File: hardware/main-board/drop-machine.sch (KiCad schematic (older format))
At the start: 29 parts, among them J1 Power in, J2 User interface, J3 Isp_conn, J4 CONN_01X06, J5 Conn_01x03, Q1 2N7000, Q2 2N7000, Q3 2N7000, Q4 2N7000, Q5 2N7000, Q6 2N7000, Q7 2N7000, SW1 On_off, U1 ATTINY2313-20PU, U2 7805

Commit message: Start with drop machine revision 2: Update to use Atmega162 that has enough pins for 19 valves. Add user interface connection with external indicator and button for flushing.
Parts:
- removed C1: 1 uF, symbol CP
- removed C2: 100 nF, symbol C
- removed J2: User interface, symbol Conn_01x03
- removed J3: Isp_conn, symbol CONN_02X03
- removed J4: CONN_01X06, symbol CONN_01X06
- removed J5: Conn_01x03, symbol Conn_01x03
- removed U1: ATTINY2313-20PU, Housings_DIP:DIP-20_W7.62mm, symbol ATTINY2313-20PU
- removed U2: 7805, symbol 7805_oturpe
- added C?: 100 nF, symbol drop-machine-rescue:C
- added C?: 330 nF, symbol drop-machine-rescue:C
- added C?: C, symbol drop-machine-rescue:C
- added C? (x2): 12 pF, symbol drop-machine-rescue:C
- added J?: Valves, symbol drop-machine-rescue:Conn_02x13_Counter_Clockwise
- added J?: CAN bus, symbol drop-machine-rescue:Screw_Terminal_1x02
- added J?: User interface, symbol Connector:Conn_01x06_Male
- added P?: isp_interface, symbol oturpe-kicad-lib:isp_interface
- added Q? (x12): 2N7000, symbol drop-machine-rescue:Q_NMOS_SGD
- added R?: R, symbol drop-machine-rescue:R
- added R? (x12): 100, symbol drop-machine-rescue:R
- added R?: 10k, symbol Device:R
- added U?: ATMEGA162-16PU, DIL40, symbol drop-machine-rescue:ATMEGA162-16PU
- added U?: MCP2515-I/ST, Housings_SSOP:TSSOP-20_4.4x6.5mm_Pitch0.65mm, symbol drop-machine-rescue:MCP2515-I_ST
- added U?: MCP2551-I/P, Housings_DIP:DIP-8_W7.62mm, symbol drop-machine-rescue:MCP2551-I_P
- added U?: 7805_oturpe, symbol oturpe-kicad-lib:7805_oturpe
- added Y?: 6 Mhz, symbol drop-machine-rescue:Crystal
- C3: symbol C -> drop-machine-rescue:C
- D1: symbol D -> drop-machine-rescue:D
- D2: symbol LED -> drop-machine-rescue:LED
- J1: symbol Screw_Terminal_1x02 -> drop-machine-rescue:Screw_Terminal_1x02
- Q1, Q2, Q3, Q4, Q5, Q6, Q7: symbol Q_NMOS_SGD -> drop-machine-rescue:Q_NMOS_SGD
- R1, R2, R3, R4, R5, R6, R7, R8, R9: symbol R -> drop-machine-rescue:R
- SW1: symbol SW_SPST-RESCUE-drop-machine -> drop-machine-rescue:SW_SPST-RESCUE-drop-machine
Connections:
- net +12V: now also C?.1, U?.1 (VI)
- net +5V: now also C?.1, P?.2 (Vcc), R?.1, R?.2, U?.20 (VDD), U?.3 (VDD), U?.3 (VO), U?.40 (VCC)
- net GND: now also C?.2, C?.2, C?.2, C?.2, C?.2, J?.1 (Pin_1), J?.14 (Pin_14), J?.15 (Pin_15), J?.17 (Pin_17), J?.19 (Pin_19), J?.21 (Pin_21), J?.23 (Pin_23), J?.25 (Pin_25), P?.6 (GND), Q?.1 (S), Q?.1 (S), Q?.1 (S), Q?.1 (S), Q?.1 (S), Q?.1 (S), Q?.1 (S), Q?.1 (S), Q?.1 (S), Q?.1 (S), Q?.1 (S), Q?.1 (S), U?.10 (VSS), U?.2 (GND), U?.2 (VSS), U?.20 (GND), U?.8 (Rs)
- net at R1.2, R2.2: now also U?.30 (PE1(ALE))
- net U1.0: now reaches Q1.3 (D)
- net U1.0: now also J?.2 (Pin_2)
- net U1.1: now reaches Q2.3 (D)
- net U1.1: now also J?.3 (Pin_3)
- net U1.2: now reaches Q3.3 (D)
- net U1.2: now also J?.4 (Pin_4)
- net U1.3: now reaches Q4.3 (D)
- net U1.3: now also J?.5 (Pin_5)
- net U1.4: now reaches Q5.3 (D)
- net U1.4: now also J?.6 (Pin_6)
- net at R1.1: now also J?.2 (Pin_2)
- net U1.5: now reaches Q6.3 (D)
- net U1.5: now also J?.7 (Pin_7)
- net U0.0: now reaches Q7.3 (D)
- net U0.0: now also J?.1 (Pin_1)
- net V0 renamed V1.0
- net V1.0: now also U?.3 ((RXD1/AIN0)PB2)
- net V1 renamed V1.1
- net V1.1: now also U?.4 ((TXD1/AIN1)PB3)
- net V2 renamed V1.2
- net V1.2: now also U?.21 ((PCINT8/A8)PC0)
- net V3 renamed V1.3
- net V1.3: now also U?.22 ((PCINT9/A9)PC1)
- net V4 renamed V1.4
- net V1.4: now also U?.23 ((PCINT10/A10)PC2)
- net V5 renamed V1.5
- net V1.5: now also U?.24 ((PCINT11/A11)PC3)
- net V6 renamed V0.0
- net V0.0: now also U?.2 ((OC2/T1)PB1)
- new net: U?.1 ((OC0/T0)PB0), U?.9 (OSC1)
- new net: C?.1, U?.18 (XTAL2), Y?.1
- new net: C?.1, U?.19 (XTAL1), Y?.2
- new net: J?.3 (Pin_3), U?.29 (PE2(OC1B))
- new net: P?.5 (Reset), U?.9 (~RESET)
- new net: U?.1 (TXCAN), U?.1 (TXD)
- new net: C?.1, R?.2, U?.19 (~RESET)
- new net: U?.2 (RXCAN), U?.4 (RXD)
- new net: Q?.2 (G), R?.2 (x12)
- new net: J?.2, U?.6 (CANL)
- new net: J?.1, U?.7 (CANH)
- new net MISO: P?.1 (MISO), U?.17 (SO), U?.7 ((MISO)PB6)
- new net MOSI: P?.4 (MOSI), U?.16 (SI), U?.6 ((MOSI)PB5)
- new net SCK: P?.3 (SCK), U?.14 (SCK), U?.8 ((SCK)PB7)
- new net U2.0: J?.8 (Pin_8), Q?.3 (D)
- new net U2.1: J?.9 (Pin_9), Q?.3 (D)
- new net U2.10: J?.18 (Pin_18), Q?.3 (D)
- new net U2.11: J?.16 (Pin_16), Q?.3 (D)
- new net U2.2: J?.10 (Pin_10), Q?.3 (D)
- new net U2.3: J?.11 (Pin_11), Q?.3 (D)
- new net U2.4: J?.12 (Pin_12), Q?.3 (D)
- new net U2.5: J?.13 (Pin_13), Q?.3 (D)
- new net U2.6: J?.26 (Pin_26), Q?.3 (D)
- new net U2.7: J?.24 (Pin_24), Q?.3 (D)
- new net U2.8: J?.22 (Pin_22), Q?.3 (D)
- new net U2.9: J?.20 (Pin_20), Q?.3 (D)
- new net V2.0: R?.1, U?.25 ((PCINT12/TCK/A12)PC4)
- new net V2.1: R?.1, U?.26 ((PCINT13/TMS/A13)PC5)
- new net V2.10: R?.1, U?.16 ((~WR~)PD6)
- new net V2.11: R?.1, U?.17 ((~RD~)PD7)
- new net V2.2: R?.1, U?.27 ((PCINT14/TDO/A14)PC6)
- new net V2.3: R?.1, U?.28 ((PCINT15/TDI/A15)PC7)
- new net V2.4: R?.1, U?.10 ((RXD0)PD0)
- new net V2.5: R?.1, U?.11 ((TXD0)PD1)
- new net V2.6: R?.1, U?.12 ((XCK1/INT0)PD2)
- new net V2.7: R?.1, U?.13 ((ICP3/INT1)PD3)
- new net V2.8: R?.1, U?.14 ((XCK0/OC3A/TOSC1)PD4)
- new net V2.9: R?.1, U?.15 ((OC1A/TOSC2)PD5)
- new net ~SS: R?.1, U?.18 (~CS), U?.5 ((OC3B/~SS~)PB4)
- no-connect marks 5 -> 4
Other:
- moved on the sheet: C3, D1, D2, J1, Q1, Q2, Q3, Q4, Q5, Q6, Q7, R1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

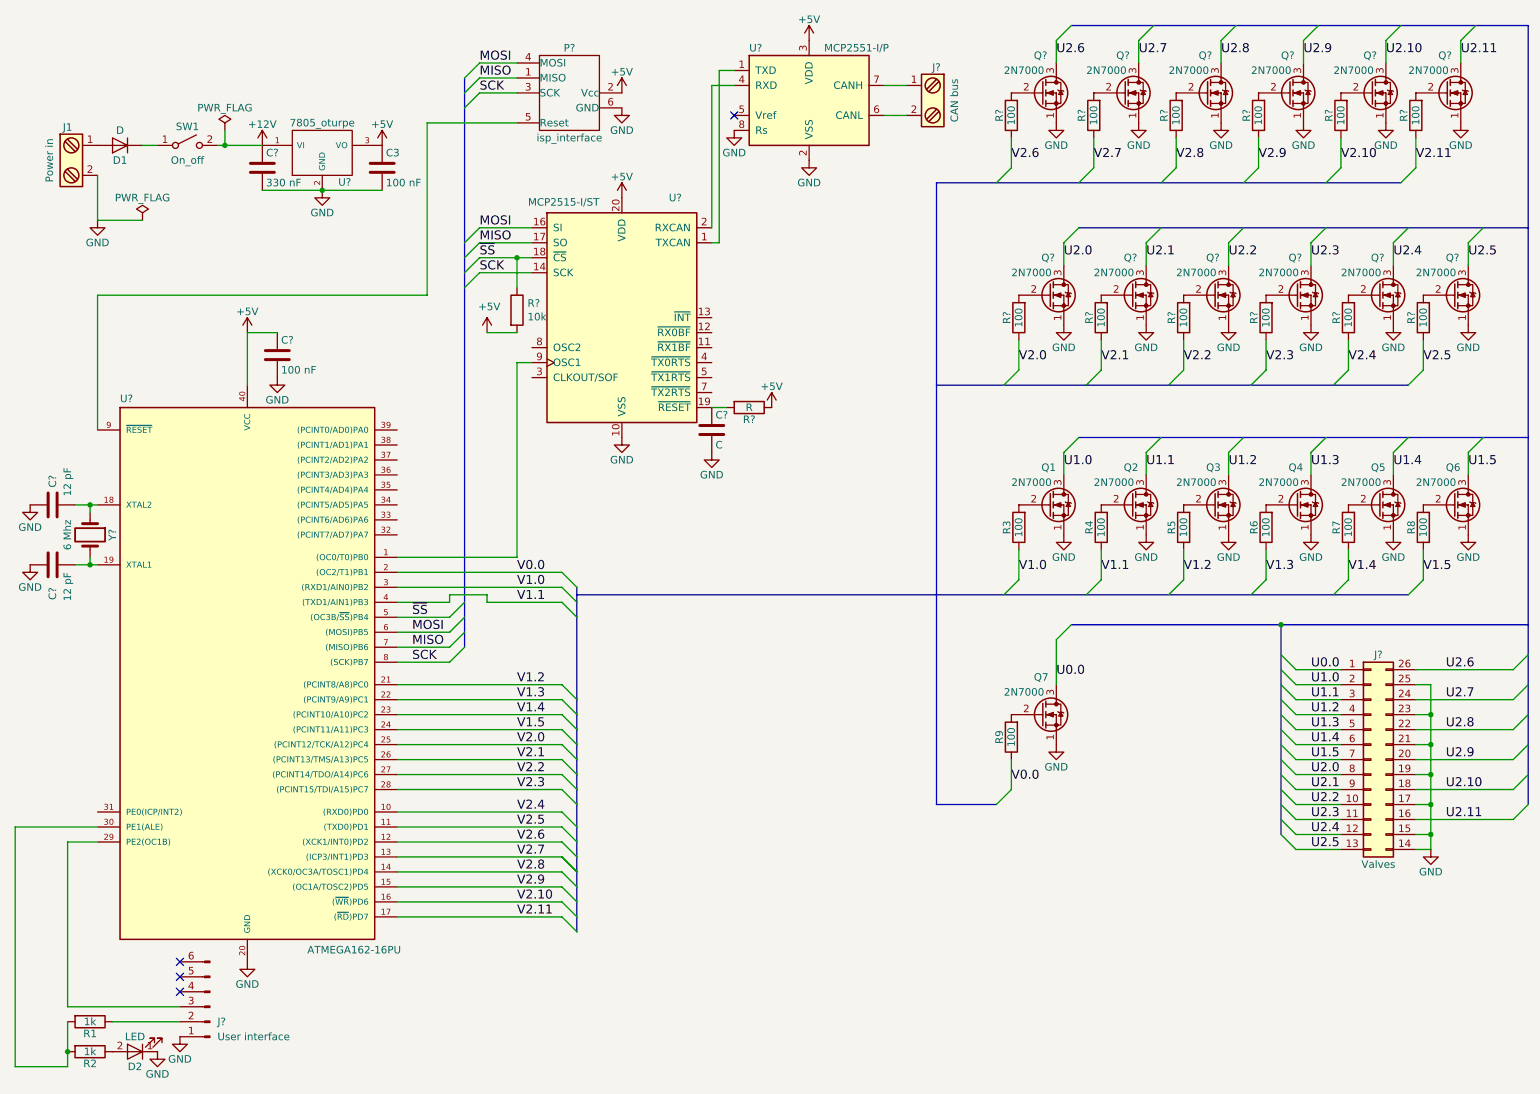
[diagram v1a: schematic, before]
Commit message: Update to fully support 19 valves
1. Fix numbering scheme of connector to match actual component used
2. Add all valves in config.h, add initialization code
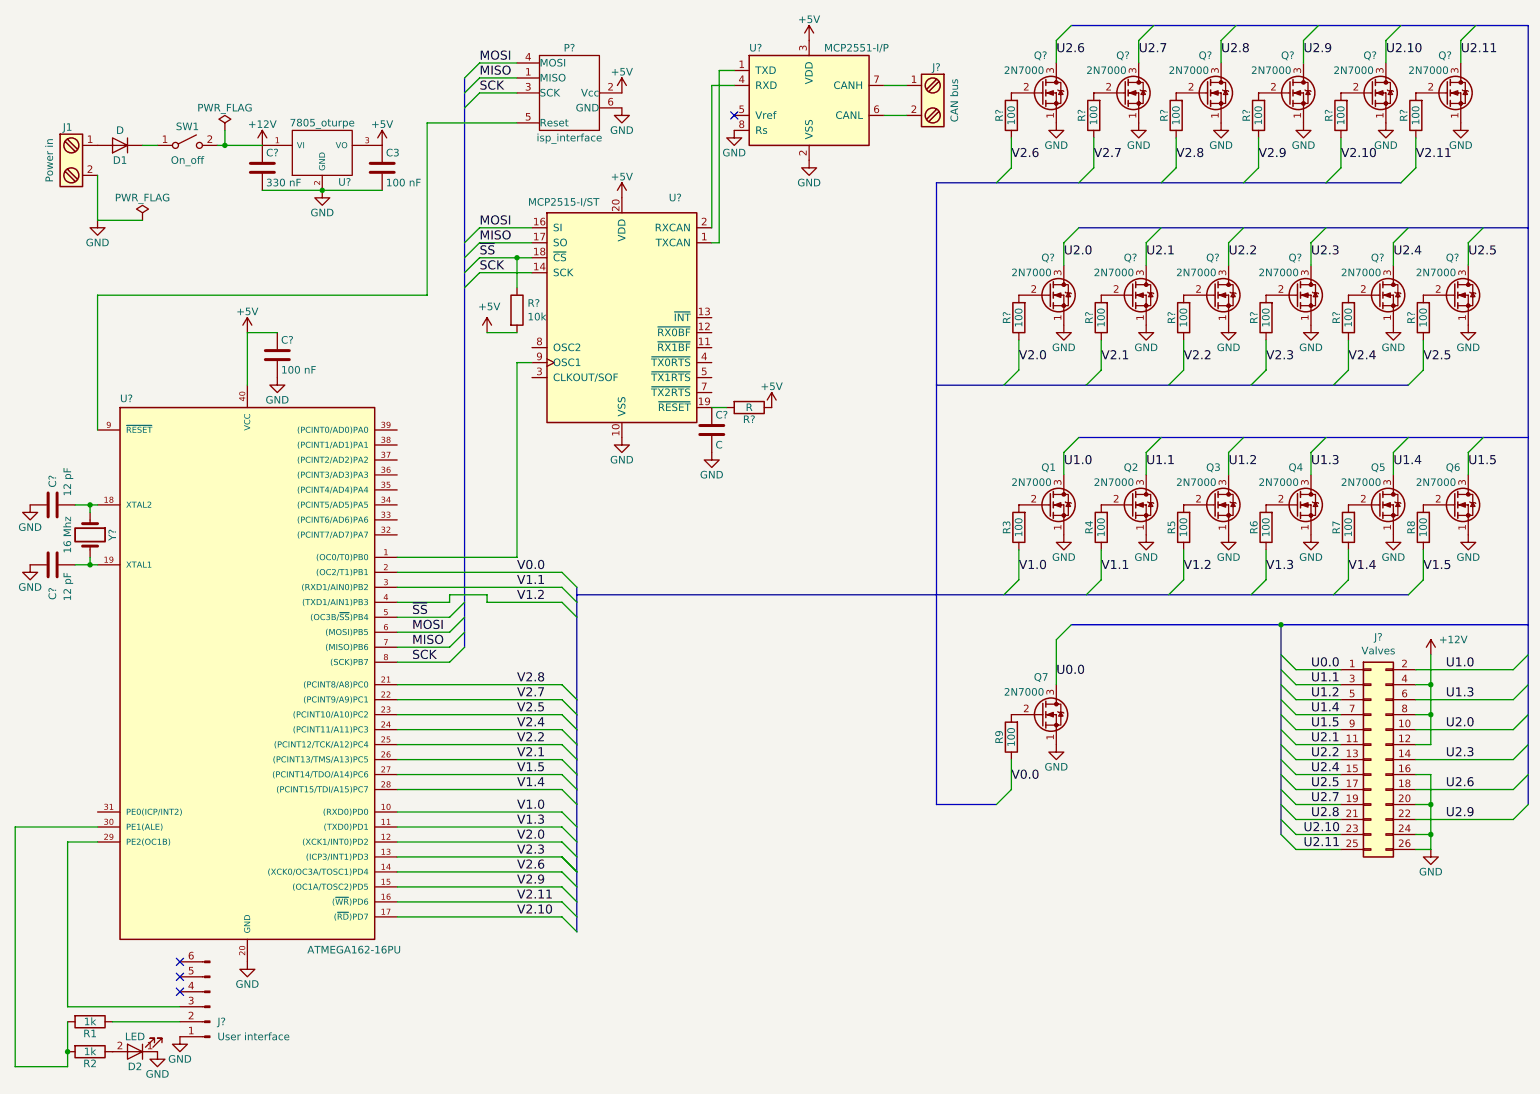
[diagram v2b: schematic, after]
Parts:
- removed J?: Valves, symbol drop-machine-rescue:Conn_02x13_Counter_Clockwise
- added J?: Valves, symbol Connector_Generic:Conn_02x13_Odd_Even
- Y?: value 6 Mhz -> 16 Mhz
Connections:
- net +12V: now also J?.12 (Pin_12), J?.4 (Pin_4), J?.8 (Pin_8)
- net GND: now also J?.16 (Pin_16), J?.20 (Pin_20), J?.24 (Pin_24), J?.26 (Pin_26)
- net U0.0: now also J?.1 (Pin_1)
- net U1.0: now also J?.2 (Pin_2)
- net U1.1: now also J?.3 (Pin_3)
- net U1.2: now also J?.5 (Pin_5)
- net U1.3: now also J?.6 (Pin_6)
- net U1.4: now also J?.7 (Pin_7)
- net U1.5: now also J?.9 (Pin_9)
- net U2.0: now also J?.10 (Pin_10)
- net U2.1: now also J?.11 (Pin_11)
- net U2.10: now also J?.23 (Pin_23)
- net U2.11: now also J?.25 (Pin_25)
- net U2.2: now also J?.13 (Pin_13)
- net U2.3: now also J?.14 (Pin_14)
- net U2.4: now also J?.15 (Pin_15)
- net U2.5: now also J?.17 (Pin_17)
- net U2.6: now also J?.18 (Pin_18)
- net U2.7: now also J?.19 (Pin_19)
- net U2.8: now also J?.21 (Pin_21)
- net U2.9: now also J?.22 (Pin_22)
- net V1.0: now also U?.10 ((RXD0)PD0); no longer U?.3 ((RXD1/AIN0)PB2)
- net V1.1: now also U?.3 ((RXD1/AIN0)PB2); no longer U?.4 ((TXD1/AIN1)PB3)
- net V1.2: now also U?.4 ((TXD1/AIN1)PB3); no longer U?.21 ((PCINT8/A8)PC0)
- net V1.3: now also U?.11 ((TXD0)PD1); no longer U?.22 ((PCINT9/A9)PC1)
- net V1.4: now also U?.28 ((PCINT15/TDI/A15)PC7); no longer U?.23 ((PCINT10/A10)PC2)
- net V1.5: now also U?.27 ((PCINT14/TDO/A14)PC6); no longer U?.24 ((PCINT11/A11)PC3)
- net V2.0: now also U?.12 ((XCK1/INT0)PD2); no longer U?.25 ((PCINT12/TCK/A12)PC4)
- net V2.10: now also U?.17 ((~RD~)PD7); no longer U?.16 ((~WR~)PD6)
- net V2.11: now also U?.16 ((~WR~)PD6); no longer U?.17 ((~RD~)PD7)
- net V2.2: now also U?.25 ((PCINT12/TCK/A12)PC4); no longer U?.27 ((PCINT14/TDO/A14)PC6)
- net V2.3: now also U?.13 ((ICP3/INT1)PD3); no longer U?.28 ((PCINT15/TDI/A15)PC7)
- net V2.4: now also U?.24 ((PCINT11/A11)PC3); no longer U?.10 ((RXD0)PD0)
- net V2.5: now also U?.23 ((PCINT10/A10)PC2); no longer U?.11 ((TXD0)PD1)
- net V2.6: now also U?.14 ((XCK0/OC3A/TOSC1)PD4); no longer U?.12 ((XCK1/INT0)PD2)
- net V2.7: now also U?.22 ((PCINT9/A9)PC1); no longer U?.13 ((ICP3/INT1)PD3)
- net V2.8: now also U?.21 ((PCINT8/A8)PC0); no longer U?.14 ((XCK0/OC3A/TOSC1)PD4)
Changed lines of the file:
@@
 P 1150 4150
 F 0 "Y?" H 1150 4300 50  0000 C CNN
-F 1 "6 Mhz" H 1150 4000 50  0000 C CNN
+F 1 "16 Mhz" H 1150 4000 50  0000 C CNN
 F 2 "" H 1150 4150 50  0001 C CNN
 F 3 "" H 1150 4150 50  0001 C CNN
@@
 V0.0
 Text Label 4000 4500 0    60   ~ 0
-V1.0
+V1.1
 Text Label 4000 4600 0    60   ~ 0
-V1.1
+V1.2
 Text Label 4000 5150 0    60   ~ 0
-V1.2
+V2.8
 Text Label 4000 5250 0    60   ~ 0
-V1.3
+V2.7
 Text Label 4000 5350 0    60   ~ 0
-V1.4
+V2.5
 Text Label 4000 5450 0    60   ~ 0
-V1.5
+V2.4
 Text Label 4000 5550 0    60   ~ 0
-V2.0
+V2.2
 Text Label 4000 5650 0    60   ~ 0
 V2.1
 Text Label 4000 5750 0    60   ~ 0
-V2.2
+V1.5
 Text Label 4000 5850 0    60   ~ 0
+V1.4
+Text Label 4000 6000 0    60   ~ 0
+V1.0
+Text Label 4000 6100 0    60   ~ 0
+V1.3
+Text Label 4000 6200 0    60   ~ 0
+V2.0
+Text Label 4000 6300 0    60   ~ 0
 V2.3
-Text Label 4000 6000 0    60   ~ 0
-V2.4
-Text Label 4000 6100 0    60   ~ 0
-V2.5
-Text Label 4000 6200 0    60   ~ 0
+Text Label 4000 6400 0    60   ~ 0
 V2.6
-Text Label 4000 6300 0    60   ~ 0
-V2.7
-Text Label 4000 6400 0    60   ~ 0
-V2.8
 Text Label 4000 6500 0    60   ~ 0
 V2.9
 Text Label 4000 6600 0    60   ~ 0
+V2.11
+Text Label 4000 6700 0    60   ~ 0
 V2.10
-Text Label 4000 6700 0    60   ~ 0
-V2.11
 Wire Bus Line
 	6800 5950 7200 5950
@@
 Wire Wire Line
 	10000 5550 10100 5550
-Connection ~ 10100 5550
 Wire Wire Line
 	10000 5750 10100 5750
-Connection ~ 10100 5750
 Wire Wire Line
 	10000 5950 10100 5950
@@
 Text Label 9300 5050 0    60   ~ 0
 U0.0
-$Comp
-L drop-machine-rescue:Conn_02x13_Counter_Clockwise J?
-U 1 1 5B9EBB2F
-P 9700 5650
-F 0 "J?" H 9750 6350 50  0000 C CNN
-F 1 "Valves" H 9750 4950 50  0000 C CNN
-F 2 "" H 9700 5650 50  0001 C CNN
-F 3 "" H 9700 5650 50  0001 C CNN
-	1    9700 5650
-	1    0    0    -1
-$EndComp
 Text Label 9300 5150 0    60   ~ 0
+U1.1
+Text Label 9300 5250 0    60   ~ 0
+U1.2
+Text Label 9300 5350 0    60   ~ 0
+U1.4
+Text Label 9300 5450 0    60   ~ 0
+U1.5
+Text Label 9300 5550 0    60   ~ 0
+U2.1
+Text Label 9300 5650 0    60   ~ 0
+U2.2
+Text Label 9300 5750 0    60   ~ 0
+U2.4
+Text Label 9300 5850 0    60   ~ 0
+U2.5
+Text Label 9300 5950 0    60   ~ 0
+U2.7
+Text Label 9300 6050 0    60   ~ 0
+U2.8
+Text Label 9250 6150 0    60   ~ 0
+U2.10
+Text Label 9250 6250 0    60   ~ 0
+U2.11
+Text Label 10200 5050 0    60   ~ 0
 U1.0
-Text Label 9300 5250 0    60   ~ 0
-U1.1
-Text Label 9300 5350 0    60   ~ 0
-U1.2
-Text Label 9300 5450 0    60   ~ 0
+Text Label 10200 5250 0    60   ~ 0
 U1.3
-Text Label 9300 5550 0    60   ~ 0
-U1.4
-Text Label 9300 5650 0    60   ~ 0
-U1.5
-Text Label 9300 5750 0    60   ~ 0
+Text Label 10200 5450 0    60   ~ 0
 U2.0
-Text Label 9300 5850 0    60   ~ 0
-U2.1
-Text Label 9300 5950 0    60   ~ 0
-U2.2
-Text Label 9300 6050 0    60   ~ 0
+Text Label 10200 5650 0    60   ~ 0
 U2.3
-Text Label 9300 6150 0    60   ~ 0
-U2.4
-Text Label 9300 6250 0    60   ~ 0
-U2.5
-Text Label 10200 5050 0    60   ~ 0
+Text Label 10200 5850 0    60   ~ 0
 U2.6
-Text Label 10200 5250 0    60   ~ 0
-U2.7
-Text Label 10200 5450 0    60   ~ 0
-U2.8
-Text Label 10200 5650 0    60   ~ 0
+Text Label 10200 6050 0    60   ~ 0
 U2.9
-Text Label 10200 5850 0    60   ~ 0
-U2.10
-Text Label 10200 6050 0    60   ~ 0
-U2.11
 Wire Wire Line
 	4000 3000 4100 3000
@@
 	10100 5350 10100 5550
 Wire Wire Line
-	10100 5550 10100 5750
-Wire Wire Line
 	10100 5750 10100 5950
 Wire Wire Line
@@
 NoConn ~ 1750 7100
 NoConn ~ 1750 7000
+$Comp
+L power:+12V #PWR?
+U 1 1 5C540623
+P 10100 4950
+F 0 "#PWR?" H 10100 4800 50  0001 C CNN
+F 1 "+12V" H 10250 5050 50  0000 C CNN
+F 2 "" H 10100 4950 50  0001 C CNN
+F 3 "" H 10100 4950 50  0001 C CNN
+	1    10100 4950
+	1    0    0    -1
+$EndComp
+Wire Wire Line
+	10100 5150 10100 4950
+Connection ~ 10100 5150
 Wire Bus Line
 	4400 4550 9950 4550
@@
 Wire Bus Line
 	4400 4500 4400 6800
+$Comp
+L Connector_Generic:Conn_02x13_Odd_Even J?
+U 1 1 5C949878
+P 9700 5650
+F 0 "J?" H 9750 6467 50  0000 C CNN
+F 1 "Valves" H 9750 6376 50  0000 C CNN
+F 2 "" H 9700 5650 50  0001 C CNN
+F 3 "~" H 9700 5650 50  0001 C CNN
+	1    9700 5650
+	1    0    0    -1
+$EndComp
 $EndSCHEMATC
